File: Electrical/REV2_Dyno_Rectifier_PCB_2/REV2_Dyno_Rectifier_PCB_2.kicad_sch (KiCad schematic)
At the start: 34 parts, among them J1 Dynamo Input, J2 Barrel_Jack_MountingPin, U1 TPS63070RNMR, U2 PAM2803AAF095

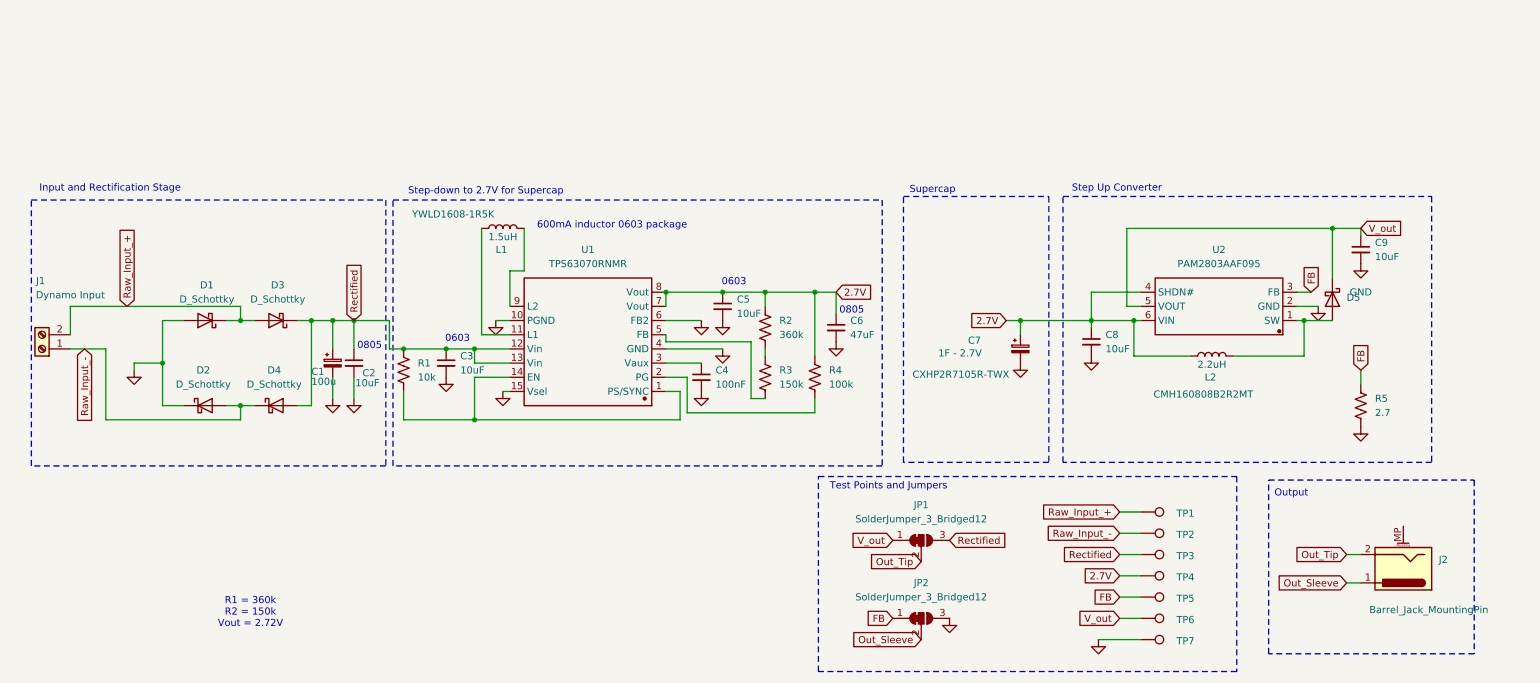
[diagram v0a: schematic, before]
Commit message: schematic should be done! component placement almost done
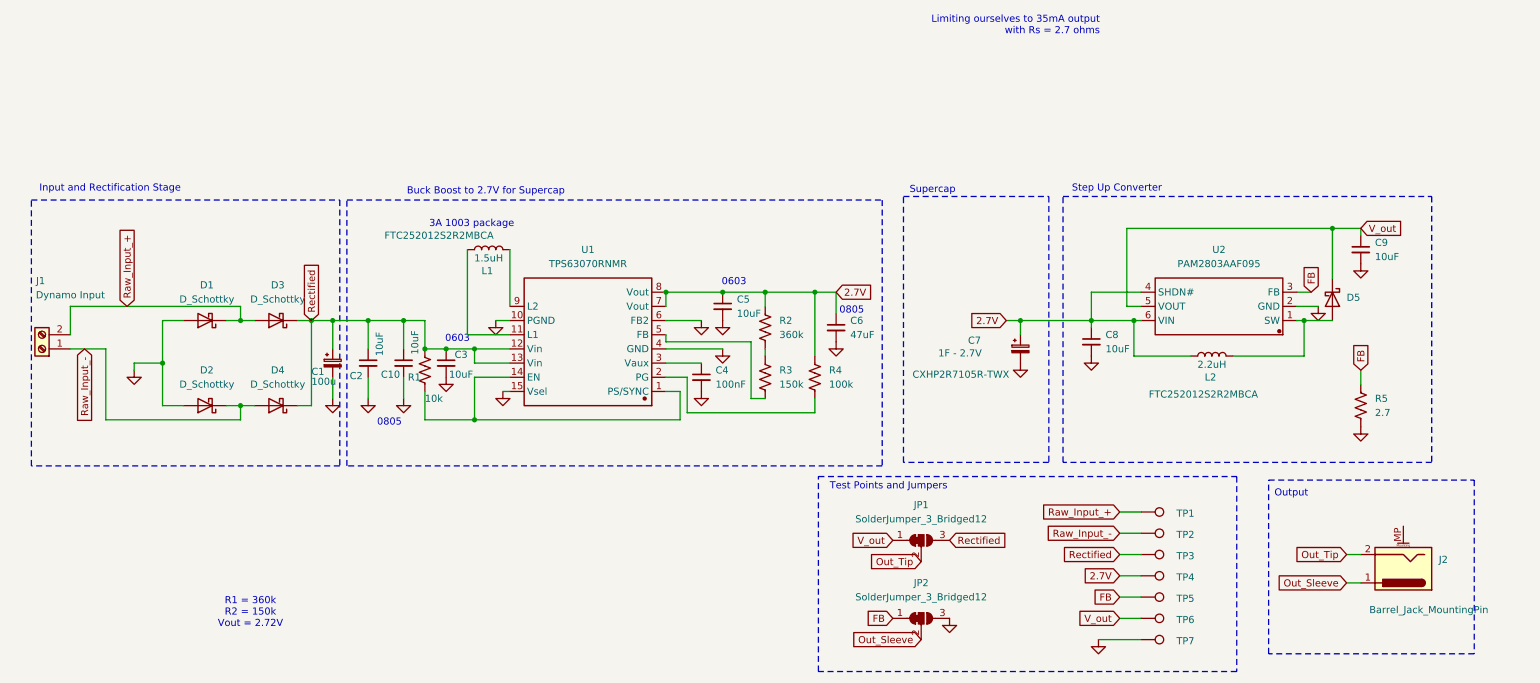
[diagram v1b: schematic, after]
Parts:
- added C10: 10uF, Capacitor_SMD:C_0805_2012Metric, symbol Device:C_Small
- C1: LCSC C3338 -> C440198
- C2, C4: LCSC (none) -> C96446
- C3: LCSC (none) -> C14663
- C5: LCSC (none) -> C16780
- C7, C8: LCSC (none) -> C440198
- C9: LCSC (none) -> C108360
- D1, D2, D3, D4, D5: LCSC C8570 -> C2886012
- L1: footprint Inductor_SMD:L_0603_1608Metric -> Inductor_SMD:L_1008_2520Metric; LCSC (none) -> C5339200; part number YWLD1608-1R5K -> FTC252012S2R2MBCA
- L2: footprint Inductor_SMD:L_0603_1608Metric -> Inductor_SMD:L_1008_2520Metric; LCSC (none) -> C394950; Part Number CMH160808B2R2MT -> FTC252012S2R2MBCA
- R1: LCSC (none) -> C25744
- R2: LCSC (none) -> C2909351
- R3: LCSC (none) -> C2909320
- R4: LCSC (none) -> C25741
- R5: LCSC (none) -> C2998159
- U1: LCSC (none) -> C109322
- U2: LCSC (none) -> C55801
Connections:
- net GND: now also D2.2 (A), C10.2; no longer D2.1 (K)
- net Raw_Input_-: now also D2.1 (K), D4.2 (A); no longer D2.2 (A), D4.1 (K)
- net Rectified: now also D4.1 (K), C10.1; no longer D4.2 (A)
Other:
- note added: "3A 1003 package"
- note added: "Buck Boost to 2.7V for Supercap"
- note added: "Limiting ourselves to 35mA output with Rs = 2.7 ohms"
- note removed: "600mA inductor 0603 package"
- note removed: "Step-down to 2.7V for Supercap"
- moved on the sheet: C2, D2, D4, L1, R1

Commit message: sent off rectifier PCB and the Light PCB off to JLCPCB tonight
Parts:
- C1: LCSC C440198 -> C108360
- C10, C2: LCSC C96446 -> C440198
- C3: LCSC C14663 -> C96446
- C4: LCSC C96446 -> C14663
- C5: LCSC C16780 -> C96446
- C6: LCSC (none) -> C16780
- C9: LCSC C108360 -> C440198
- R5: value 2.7 -> 1.8; LCSC C2998159 -> C2960794
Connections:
- net Out_Sleeve: now also J2.2; no longer J2.1
- net Out_Tip: now also J2.1; no longer J2.2
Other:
- note added: "Limiting ourselves to 52mA output with Rs = 1.8 ohms"
- note removed: "Limiting ourselves to 35mA output with Rs = 2.7 ohms"
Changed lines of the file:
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@@
 		)
 	)
-	(text "Limiting ourselves to 35mA output \nwith Rs = 2.7 ohms"
+	(text "Limiting ourselves to 52mA output \nwith Rs = 1.8 ohms"
 		(exclude_from_sim no)
 		(at 209.804 38.608 0)
@@
 	(global_label "Out_Tip"
 		(shape input)
-		(at 254 133.35 180)
+		(at 254 138.43 180)
 		(fields_autoplaced yes)
 		(effects
@@
 		)
 		(property "Intersheetrefs" "${INTERSHEET_REFS}"
-			(at 244.1206 133.35 0)
+			(at 244.1206 138.43 0)
 			(effects
 				(font
@@
 	(global_label "Out_Sleeve"
 		(shape input)
-		(at 254 138.43 180)
+		(at 254 133.35 180)
 		(fields_autoplaced yes)
 		(effects
@@
 		)
 		(property "Intersheetrefs" "${INTERSHEET_REFS}"
-			(at 240.7339 138.43 0)
+			(at 240.7339 133.35 0)
 			(effects
 				(font
@@
 			)
 		)
-		(property "LCSC" "C14663"
+		(property "LCSC" "C96446"
 			(at 95.25 97.7962 0)
 			(effects
@@
 			)
 		)
-		(property "LCSC" "C96446"
+		(property "LCSC" "C14663"
 			(at 140.97 100.3362 0)
 			(effects
@@
 			)
 		)
-		(property "LCSC" "C96446"
+		(property "LCSC" "C440198"
 			(at 86.614 100.838 0)
 			(effects
@@
 			)
 		)
+		(property "LCSC" "C16780"
+			(at 165.1 91.4462 0)
+			(effects
+				(font
+					(size 1.27 1.27)
+				)
+				(hide yes)
+			)
+		)
 		(pin "1"
 		)
@@
 			)
 		)
-		(property "LCSC" "C108360"
+		(property "LCSC" "C440198"
 			(at 259.08 77.4762 0)
 			(effects
@@
 			)
 		)
-		(property "LCSC" "C440198"
+		(property "LCSC" "C108360"
 			(at 74.93 97.2438 0)
 			(effects
@@
 			)
 		)
-		(property "Value" "2.7"
+		(property "Value" "1.8"
 			(at 259.08 107.9499 0)
 			(effects
@@
 			)
 		)
-		(property "LCSC" "C2998159"
+		(property "LCSC" "C2960794"
 			(at 259.08 105.4099 0)
 			(effects
@@
 			)
 		)
-		(property "LCSC" "C16780"
+		(property "LCSC" "C96446"
 			(at 144.78 87.6362 0)
 			(effects
@@
 			)
 		)
-		(property "LCSC" "C96446"
+		(property "LCSC" "C440198"
 			(at 80.264 100.838 0)
 			(effects

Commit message: V2 is (pretty much) done! need to organize things better but it is all here!
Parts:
- L1: part number FTC252012S2R2MBCA -> FTC252012S1R5MBCA
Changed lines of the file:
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@@
 			)
 		)
-		(property "part number" "FTC252012S2R2MBCA"
+		(property "part number" "FTC252012S1R5MBCA"
 			(at 91.44 76.2 90)
 			(effects
